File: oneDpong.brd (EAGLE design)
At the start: 136.4 x 80 mm, 66 parts, among them IC1 MEGA8-AI, IC2 74HC257D, IC3 LM386M-1, IC4 NPIC6C596, IC5 NPIC6C596

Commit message: pcb ready
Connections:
- net GND: now also ICSP.6; no longer ICSP.3
- net N$2: now also ICSP.1; no longer ICSP.5
- net N$7: now also ICSP.3; no longer ICSP.6
- net RST0: now also ICSP.5; no longer ICSP.1
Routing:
- net N$7: track 42.5 -> 34.8 mm, vias 2 -> 0
- net GND: track 79.7 -> 85.5 mm, vias 0 -> 2
- net N$2: track 6.41 -> 9.32 mm, vias 0 -> 2
- net RST0: track 45.0 -> 44.0 mm
- net N$13: track 35.8 -> 36.3 mm

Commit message: stuff
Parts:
- removed C14: (no value), rcl:C0805
- removed GND1, GND2, VCC1, VCC2: (no value), pinhead:1X01
- added C15: (no value), rcl:C0805
- added R18: (no value), rcl:R0805
- moved SPK+ 70.7 mm to (58.4, 83.8)
- moved SPK- 70.7 mm to (61.0, 83.8)
- moved RST 68.1 mm to (72.4, 83.8)
- moved RST_GND 68.1 mm to (74.9, 83.8)
- moved JP1 46.8 mm to (15.2, 47.0), turned to 270 degrees
- moved C8 45.5 mm to (59.7, 73.7), turned to 90 degrees
- moved SW_GND1 16.5 mm to (96.5, 10.2)
- moved SW_GND2 13.1 mm to (99.1, 10.2)
- moved SW1 7.87 mm to (82.3, 16.5)
- moved 5V 7.62 mm to (125.7, 16.5)
- moved C12 6.35 mm to (66.0, 73.7)
- moved GND 5.08 mm to (123.2, 16.5)
- moved P1GND 5.08 mm to (66.0, 16.5)
- moved PLAYER1 5.08 mm to (63.5, 16.5)
- moved SW2 4.06 mm to (79.8, 16.5)
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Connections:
- new net N$25: C11.2, R18.1
- new net N$9: C15.2, JP1.1
- net GND: no longer GND1.1, GND2.1
- net N$16: now also R18.2; no longer C11.2
- net RESET: now also C15.1, IC1.29, R9.1; no longer C14.2, JP1.1
- net RST0: no longer C14.1, IC1.29, R9.1
- net VCC: no longer VCC1.1, VCC2.1
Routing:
- net VCC: track 321.7 -> 222.9 mm
- net N$19: track 93.6 -> 3.90 mm
- net N$14: track 32.3 -> 8.56 mm
- net N$1: track 38.4 -> 19.9 mm
- net N$20: track 16.5 -> 0.00 mm
- net SW1: track 12.8 -> 1.48 mm
- net RESET: track 7.39 -> 0.00 mm
- net N$18: track 7.42 -> 1.70 mm
- net N$16: track 5.18 -> 0.00 mm
- net N$17: track 7.82 -> 4.38 mm
- net RST0: track 44.0 -> 41.9 mm
- net Q4A1: track 29.3 -> 29.8 mm
- net Q3A1: track 20.6 -> 21.1 mm
- net Q2A1: track 20.6 -> 21.1 mm
- net Q1A1: track 22.2 -> 22.7 mm
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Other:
- board text added: "mainboard rev 2"
- board text removed: "mainboard rev 1"

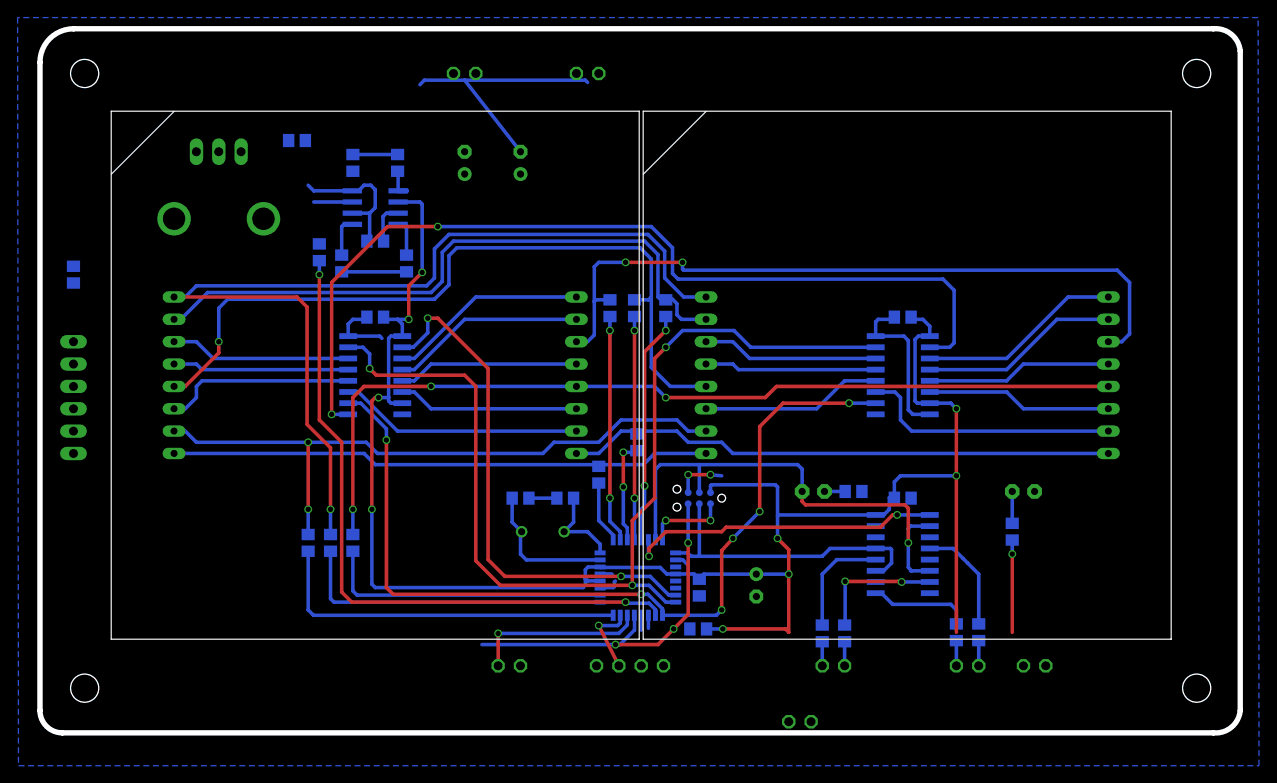
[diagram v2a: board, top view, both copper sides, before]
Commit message: add overvoltage protect, refactor
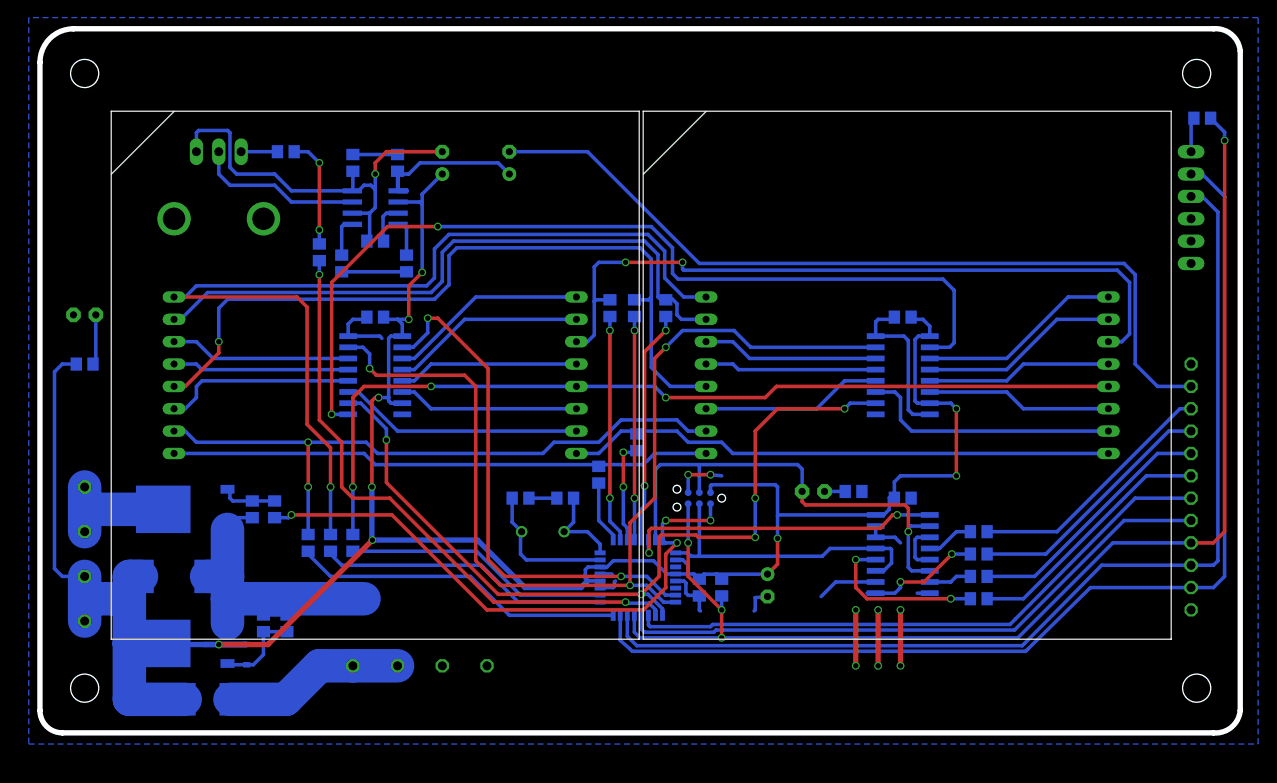
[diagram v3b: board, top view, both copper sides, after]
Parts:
- removed 5V, P1GND, P2GND, RST_GND, SPK-, SW_GND1, SW_GND2: (no value), pinhead:1X01
- added 5VA, 5VA1, 5VA2, 5VA3, 5VA4, 5VB, GND1, GNDA, GNDB: (no value), pinhead:1X01
- added C14: (no value), rcl:C0805
- added D1: (no value), diode:SMC
- added D2: DIODE-ZENER-BZT52, SparkFun:SOD-323
- added PTC1: (no value), microbuilder:PTC1812
- added Q2: NTD5867NL_NMOSFET, jason_eagle6:DPACK
- added Q3: SCR_BT300S, jason_eagle6:DPACK
- added R19, R20, R21: (no value), rcl:R0805
- moved C15 129.5 mm to (143.5, 78.7), turned to 0 degrees
- moved JP1 128.8 mm to (142.2, 68.6)
- moved PWR 108.6 mm to (16.5, 56.4), turned to 0 degrees
- moved R17 107.1 mm to (16.5, 50.8), turned to 0 degrees
- moved SPK+ 91.1 mm to (142.2, 48.3)
- moved RST 87.9 mm to (142.2, 30.5)
- moved PLAYER1 79.6 mm to (142.2, 27.9)
- moved PLAYER2 65.6 mm to (142.2, 25.4)
- moved SW2 64.6 mm to (142.2, 33.0)
- moved SW1 62.9 mm to (142.2, 35.6)
- moved SCK2 47.1 mm to (142.2, 38.1)
- moved MOSI2 46.2 mm to (142.2, 40.6)
- moved GND 39.2 mm to (142.2, 50.8)
- moved MOSI1 37.9 mm to (142.2, 45.7)
- moved SCK1 37.7 mm to (142.2, 43.2)
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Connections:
- removed net N$2: IC1.16, ICSP.1
- removed net RST0: ICSP.5
- new net ENA_STRIP: IC1.16, ICSP.1, R21.1
- new net N$28: 5VA.1, 5VB.1, PTC1.P$2
- new net N$31: C14.1, D2.2, Q3.3, R19.1
- new net N$32: 5VA3.1, 5VA4.1, Q2.2
- new net Z: Q2.1, R20.1, R21.2
- net GND: now also C14.2, D1.A, GND1.1, GNDA.1, GNDB.1, Q2.3, Q3.1, R19.2, R20.2; no longer P1GND.1, P2GND.1, RST_GND.1, SPK-.1, SW_GND1.1, SW_GND2.1
- net RESET: now also ICSP.5
- net VCC: now also 5VA1.1, 5VA2.1, D1.C, D2.1, PTC1.P$1, Q3.2; no longer 5V.1
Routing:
- net RESET: track 0.00 -> 140.3 mm, vias 0 -> 4
- net N$14: track 8.56 -> 123.5 mm, vias 1 -> 0
- net N$1: track 19.9 -> 117.4 mm, vias 1 -> 0
- net N$20: track 0.00 -> 94.5 mm
- net GND: track 85.2 -> 171.3 mm, vias 2 -> 9
- net VCC: track 222.9 -> 291.1 mm, vias 10 -> 9
- net N$18: track 1.70 -> 69.4 mm
- net SW1: track 1.48 -> 68.9 mm
- net ENA_STRIP: track 0.00 -> 66.8 mm, vias 0 -> 4
- net RST0: track 41.9 -> 0.00 mm, vias 3 -> 0
- net N$15: track 2.73 -> 29.0 mm
- net MOSI2: track 2.73 -> 29.0 mm
- net SCK1: track 2.86 -> 29.0 mm
- net N$12: track 2.86 -> 29.0 mm
- net N$28: track 0.00 -> 21.1 mm
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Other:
- board text added: "C1"
- board text added: "C2"
- board text added: "D1"
- board text added: "D2"
- board text added: "GD"
- board text added: "GND"
- board text added: "INPUT/OUTPUT"
- board text added: "P1"
- board text added: "P2"
- board text added: "RT"
- board text added: "S1"
- board text added: "S2"
- board text added: "SERIAL PROG"
- board text added: "SP"
- board text added: "STRIP"
- board text added: "SUPPLY IN"
- board text removed: "+"
- board text removed: "-"
- board text removed: "0V"
- board text removed: "1"
- board text removed: "CK"
- board text removed: "PLA"
- board text removed: "PLB"
- board text removed: "POWER"
- board text removed: "RST"
- board text removed: "SD"
- board text removed: "SERIAL"
- board text removed: "SPK"
- board text removed: "STRIP1"
- board text removed: "STRIP2"
- board text removed: "SWA"
- board text removed: "SWB"

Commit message: tweaks
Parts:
- removed 5VA1, 5VA3, GNDA, GNDB: (no value), pinhead:1X01
- moved PWR 10.2 mm to (16.5, 46.2)
- moved R17 10.2 mm to (16.5, 40.6)
- renumbered 5VA to 5V, 5VB to GND_
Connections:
- net GND: now also GND_.1; no longer GNDA.1, GNDB.1
- net N$28: no longer GND_.1
- net N$32: no longer 5VA3.1
- net VCC: no longer 5VA1.1
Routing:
- net VCC: track 291.1 -> 268.3 mm
- net N$28: track 21.1 -> 16.0 mm
- net N$32: track 14.0 -> 11.5 mm
- net GND: track 171.3 -> 169.0 mm

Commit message: bits
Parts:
- C11, C14, C9: value (none) -> 100n
- C7: value (none) -> 47n
- R1, R12, R13, R14, R15, R19, R2, R3, R4, R5, R6, R7, R8: value (none) -> 100r
- R10: value (none) -> 10r
- R11, R21: value (none) -> 1k
- R20: value (none) -> 10k
- renumbered R18 to 100K

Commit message: tidy up values
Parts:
- renumbered 100K to R18
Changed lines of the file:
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@@
 <element name="R1" library="rcl" package="R0805" value="100r" x="76.2" y="57.15" smashed="yes" rot="MR90">
 <attribute name="NAME" x="77.216" y="59.309" size="1.27" layer="26" rot="MR0"/>
-<attribute name="VALUE" x="73.66" y="56.515" size="1.27" layer="28" rot="MR90"/>
 </element>
 <element name="R2" library="rcl" package="R0805" value="100r" x="46.99" y="30.48" smashed="yes" rot="MR90">
 <attribute name="NAME" x="48.133" y="27.178" size="1.27" layer="26" rot="MR0"/>
-<attribute name="VALUE" x="44.45" y="29.845" size="1.27" layer="28" rot="MR90"/>
 </element>
 <element name="R3" library="rcl" package="R0805" value="100r" x="79.248" y="41.91" smashed="yes" rot="MR90">
 <attribute name="NAME" x="80.264" y="43.942" size="1.27" layer="26" rot="MR0"/>
-<attribute name="VALUE" x="76.708" y="41.275" size="1.27" layer="28" rot="MR90"/>
 </element>
 <element name="R4" library="rcl" package="R0805" value="100r" x="74.93" y="38.227" smashed="yes" rot="MR90">
@@
 <element name="R5" library="rcl" package="R0805" value="100r" x="41.91" y="30.48" smashed="yes" rot="MR90">
 <attribute name="NAME" x="43.053" y="27.178" size="1.27" layer="26" rot="MR0"/>
-<attribute name="VALUE" x="39.37" y="29.845" size="1.27" layer="28" rot="MR90"/>
 </element>
 <element name="R6" library="rcl" package="R0805" value="100r" x="78.994" y="57.15" smashed="yes" rot="MR90">
 <attribute name="NAME" x="80.391" y="59.309" size="1.27" layer="26" rot="MR0"/>
-<attribute name="VALUE" x="76.454" y="56.515" size="1.27" layer="28" rot="MR90"/>
 </element>
 <element name="R7" library="rcl" package="R0805" value="100r" x="82.55" y="57.15" smashed="yes" rot="MR90">
 <attribute name="NAME" x="83.566" y="59.182" size="1.27" layer="26" rot="MR0"/>
-<attribute name="VALUE" x="80.01" y="56.515" size="1.27" layer="28" rot="MR90"/>
 </element>
 <element name="R8" library="rcl" package="R0805" value="100r" x="44.45" y="30.48" smashed="yes" rot="MR90">
 <attribute name="NAME" x="45.466" y="32.385" size="1.27" layer="26" rot="MR0"/>
-<attribute name="VALUE" x="41.91" y="29.845" size="1.27" layer="28" rot="MR90"/>
 </element>
 <element name="U$2" library="jasons_stuff" package="LARGE8X8" value="LARGE8X8" x="109.982" y="49.53"/>
@@
 </element>
 <element name="R9" library="rcl" package="R0805" value="" x="88.9" y="25.4" smashed="yes" rot="MR90">
-<attribute name="NAME" x="86.741" y="24.257" size="1.27" layer="26" rot="MR90"/>
+<attribute name="NAME" x="90.043" y="27.686" size="1.27" layer="26" rot="MR0"/>
 <attribute name="VALUE" x="86.36" y="24.765" size="1.27" layer="28" rot="MR90"/>
 </element>
@@
 <element name="R12" library="rcl" package="R0805" value="100r" x="118.11" y="31.75" smashed="yes" rot="MR0">
 <attribute name="NAME" x="120.65" y="32.131" size="1.27" layer="26" rot="MR180"/>
-<attribute name="VALUE" x="118.745" y="29.21" size="1.27" layer="28" rot="MR0"/>
 </element>
 <element name="R13" library="rcl" package="R0805" value="100r" x="118.11" y="26.67" smashed="yes" rot="MR0">
 <attribute name="NAME" x="120.523" y="27.305" size="1.27" layer="26" rot="MR180"/>
-<attribute name="VALUE" x="118.745" y="24.13" size="1.27" layer="28" rot="MR0"/>
 </element>
 <element name="R14" library="rcl" package="R0805" value="100r" x="118.11" y="29.21" smashed="yes" rot="MR0">
 <attribute name="NAME" x="120.523" y="29.718" size="1.27" layer="26" rot="MR180"/>
-<attribute name="VALUE" x="118.745" y="26.67" size="1.27" layer="28" rot="MR0"/>
 </element>
 <element name="R15" library="rcl" package="R0805" value="100r" x="118.11" y="24.13" smashed="yes" rot="MR0">
 <attribute name="NAME" x="120.523" y="24.765" size="1.27" layer="26" rot="MR180"/>
-<attribute name="VALUE" x="118.745" y="21.59" size="1.27" layer="28" rot="MR0"/>
 </element>
 <element name="MOSI1" library="pinhead" package="1X01" value="" x="142.24" y="45.72" smashed="yes" rot="MR0">
@@
 <element name="C7" library="rcl" package="C0805" value="47n" x="52.07" y="73.66" smashed="yes" rot="MR270">
 <attribute name="NAME" x="51.054" y="76.962" size="1.27" layer="26" rot="MR180"/>
-<attribute name="VALUE" x="54.61" y="74.93" size="1.27" layer="28" rot="MR270"/>
 </element>
 <element name="C8" library="rcl" package="E2,5-6" value="" x="64.77" y="73.66" smashed="yes" rot="MR90">
@@
 <element name="C11" library="rcl" package="C0805" value="100n" x="43.18" y="63.5" smashed="yes" rot="MR90">
 <attribute name="NAME" x="41.783" y="62.103" size="1.27" layer="26" rot="MR0"/>
-<attribute name="VALUE" x="40.64" y="62.23" size="1.27" layer="28" rot="MR90"/>
 </element>
 <element name="C12" library="rcl" package="E2,5-6" value="" x="57.15" y="73.66" smashed="yes" rot="MR90">
@@
 <element name="C9" library="rcl" package="C0805" value="100n" x="49.53" y="64.77" smashed="yes" rot="MR180">
 <attribute name="NAME" x="48.514" y="63.246" size="1.27" layer="26" rot="MR180"/>
-<attribute name="VALUE" x="48.26" y="67.31" size="1.27" layer="28" rot="MR180"/>
 </element>
 <element name="ICSP" library="jasons_stuff" package="TC2030-MCP-NL" value="TAG_CONN_AVR" x="88.9" y="35.56" smashed="yes" rot="MR0">
@@
 <element name="R10" library="rcl" package="R0805" value="10r" x="46.99" y="73.66" smashed="yes" rot="MR270">
 <attribute name="NAME" x="44.958" y="76.835" size="1.27" layer="26" rot="MR180"/>
-<attribute name="VALUE" x="49.53" y="74.295" size="1.27" layer="28" rot="MR270"/>
 </element>
 <element name="C15" library="rcl" package="C0805" value="" x="143.51" y="78.74" smashed="yes" rot="MR0">
@@
 <attribute name="VALUE" x="144.78" y="76.2" size="1.27" layer="28" rot="MR0"/>
 </element>
-<element name="100K" library="rcl" package="R0805" value="" x="39.37" y="74.93" rot="MR0"/>
+<element name="R18" library="rcl" package="R0805" value="" x="39.37" y="74.93" smashed="yes" rot="MR0">
+<attribute name="NAME" x="40.005" y="76.2" size="1.27" layer="26" rot="MR0"/>
+<attribute name="VALUE" x="40.005" y="72.39" size="1.27" layer="28" rot="MR0"/>
+</element>
 <element name="Q3" library="jason_eagle6" package="DPACK" value="SCR_BT300S" x="27.94" y="19.05" smashed="yes" rot="MR270">
 <attribute name="NAME" x="33.274" y="22.225" size="1.27" layer="26" rot="MR0"/>
@@
 <element name="R19" library="rcl" package="R0805" value="100r" x="36.83" y="21.336" smashed="yes" rot="MR90">
 <attribute name="NAME" x="37.973" y="23.749" size="1.27" layer="26" rot="MR0"/>
-<attribute name="VALUE" x="34.29" y="20.701" size="1.27" layer="28" rot="MR90"/>
 </element>
 <element name="5V" library="pinhead" package="1X01" value="" x="46.99" y="16.51" smashed="yes" rot="MR0">
@@
 <element name="R20" library="rcl" package="R0805" value="10k" x="35.56" y="34.29" smashed="yes" rot="MR270">
 <attribute name="NAME" x="34.29" y="32.004" size="1.27" layer="26" rot="MR180"/>
-<attribute name="VALUE" x="38.1" y="34.925" size="1.27" layer="28" rot="MR270"/>
 </element>
 <element name="C14" library="rcl" package="C0805" value="100n" x="39.497" y="21.336" smashed="yes" rot="MR90">
 <attribute name="NAME" x="41.91" y="23.749" size="1.27" layer="26" rot="MR0"/>
-<attribute name="VALUE" x="36.957" y="20.066" size="1.27" layer="28" rot="MR90"/>
 </element>
 <element name="Q2" library="jason_eagle6" package="DPACK" value="NTD5867NL_NMOSFET" x="27.94" y="34.29" smashed="yes" rot="MR270">
@@
 <element name="R21" library="rcl" package="R0805" value="1k" x="38.1" y="34.29" smashed="yes" rot="MR90">
 <attribute name="NAME" x="39.751" y="36.576" size="1.27" layer="26" rot="MR0"/>
-<attribute name="VALUE" x="35.56" y="33.655" size="1.27" layer="28" rot="MR90"/>
 </element>
 <element name="GND" library="pinhead" package="1X01" value="" x="142.24" y="50.8" smashed="yes" rot="MR0">
@@
 <signal name="N$16">
 <contactref element="VOLUME" pad="B"/>
-<contactref element="100K" pad="2"/>
+<contactref element="R18" pad="2"/>
 <wire x1="34.29" y1="74.93" x2="38.42" y2="74.93" width="0.4064" layer="16"/>
 </signal>
 <signal name="N$25">
-<contactref element="100K" pad="1"/>
+<contactref element="R18" pad="1"/>
 <contactref element="C11" pad="2"/>
 <wire x1="40.32" y1="74.93" x2="41.91" y2="74.93" width="0.4064" layer="16"/>

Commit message: poss V3
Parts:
- removed D2: DIODE-ZENER-BZT52, SparkFun:SOD-323
- removed Q3: SCR_BT300S, jason_eagle6:DPACK
- removed R19: 100r, rcl:R0805
- added C16: 1u, rcl:C0805
- added IC6: NCP361SNT1G, jason_eagle6:SOT23-5
- added R22: 100r, rcl:R0805
- added TP2: TPB2,54, testpad:B2,54
- C14: value 100n -> 1u
- moved C14 3.64 mm to (38.7, 17.8), turned to 180 degrees
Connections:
- removed net N$13: IC1.14, IC2.1
- removed net N$31: C14.1, D2.2, Q3.3, R19.1
- new net MISO: IC1.16, ICSP.1
- new net N$2: IC2.1, R22.1
- new net VIN: 5VA2.1, C14.1, D1.C, IC6.1, PTC1.P$1
- net ENA_STRIP: now also IC1.14, TP2.TP; no longer IC1.16, ICSP.1
- net GND: now also C16.2, IC6.2, IC6.3, R22.2; no longer Q3.1, R19.2
- net VCC: now also C16.1, IC6.5; no longer 5VA2.1, D1.C, D2.1, PTC1.P$1, Q3.2
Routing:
- net VIN: track 0.00 -> 44.6 mm
- net VCC: track 268.3 -> 227.3 mm, vias 9 -> 10
- net N$13: track 36.7 -> 0.00 mm, vias 2 -> 0
- net ENA_STRIP: track 66.8 -> 92.7 mm
- net GND: track 169.0 -> 146.1 mm
- net N$31: track 9.90 -> 0.00 mm
- net MISO: track 0.00 -> 9.32 mm, vias 0 -> 2
- net N$2: track 0.00 -> 4.93 mm
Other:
- board text added: "mainboard rev 3"
- board text removed: "mainboard rev 2"
